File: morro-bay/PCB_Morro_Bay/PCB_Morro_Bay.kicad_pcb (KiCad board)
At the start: 2 copper layers, 220 x 145.5 mm, 344 parts, among them J1 POWER, J10 5V_12_8, J11 5V_12_9, J12 5V_12_10, J13 5V_12_11, J14 5V_12_12, J15 5V_12_13, J16 5V_12_14, J17 10V_12_1, J18 10V_12_2, J19 10V_12_3, J2 CAN, J20 10V_12_4, J21 10V_12_5, J22 10V_12_6, J23 POWER_OUT, J24 5V_16_1, J25 5V_16_2, J26 5V_16_3, J27 5V_16_4, J28 10V_16_1, J29 10V_16_2, J3 5V_12_1, J30 10V_16_3, J31 10V_16_4, J32 5V_16_5, J33 5V_16_6, J34 5V_16_7, J35 5V_16_8, J36 SWD, J37 GPIO, J38 USB_B, J39 ESERCOM, J4 5V_12_2, J5 5V_12_3, J6 5V_12_4, J7 5V_12_5, J8 5V_12_6, J9 5V_12_7, SW1 INPUT_RANGE_SEL_1, SW2 INPUT_RANGE_SEL_2, SW3 RESET, SW4 INPUT_RANGE_SEL_3, U1 MCP2515-xSO, U10 LM2902, U11 LM2902, U12 LM2902, U13 V7805-2000R, U2 SN65HVD232, U26 ADS114S08BIPBSR, U3 AZ1117-3.3, U4 ATSAMD21J18A-AU, U5 LM2902, U6 LM2902, U7 LM2902, U8 LM2902, U9 LM2902, Y1 8MHz, Y2 30MHz, Y3 32.768kHz

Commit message: Silkscreened
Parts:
- added G***: LOGO, PCB_Morro_Bay:M_Logo, B.Cu at (199.2, 84.5)
- added G***: LOGO, PCB_Morro_Bay:P_Logo_Small, F.Cu at (235.0, 171.2)
- moved G*** 173.9 mm to (256.2, 172.8)
- moved J36 99.1 mm to (152.2, 101.6)
- moved R118 99.1 mm to (157.2, 123.8)
- moved C1 99.1 mm to (141.2, 121.8)
- moved C10 99.1 mm to (186.2, 130.2)
- moved C11 99.1 mm to (209.0, 130.2)
- moved C12 99.1 mm to (190.8, 124.2)
- moved C13 99.1 mm to (167.5, 114.5)
- moved C14 99.1 mm to (167.5, 119.0)
- moved C15 99.1 mm to (177.0, 116.8)
- moved C16 99.1 mm to (167.5, 120.8)
- moved C17 99.1 mm to (168.5, 128.8)
- moved C18 99.1 mm to (170.5, 135.2)
- moved C19 99.1 mm to (168.8, 135.2)
- moved C2 99.1 mm to (161.0, 118.2)
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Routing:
- net /SAMD_nRESET: track 45.9 -> 46.9 mm
- net GND: vias 208 -> 209
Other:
- board text added: "Morro Bay SN: Data Acquisition Board"
- board text removed: "Morro Bay Data Acquisition Board"

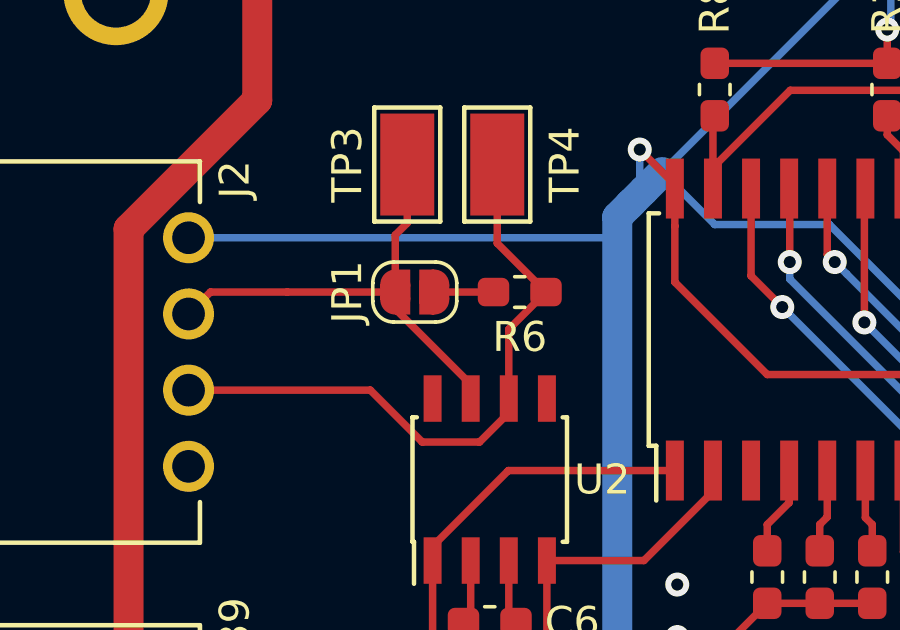
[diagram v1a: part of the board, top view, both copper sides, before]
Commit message: Add CAN termination marking
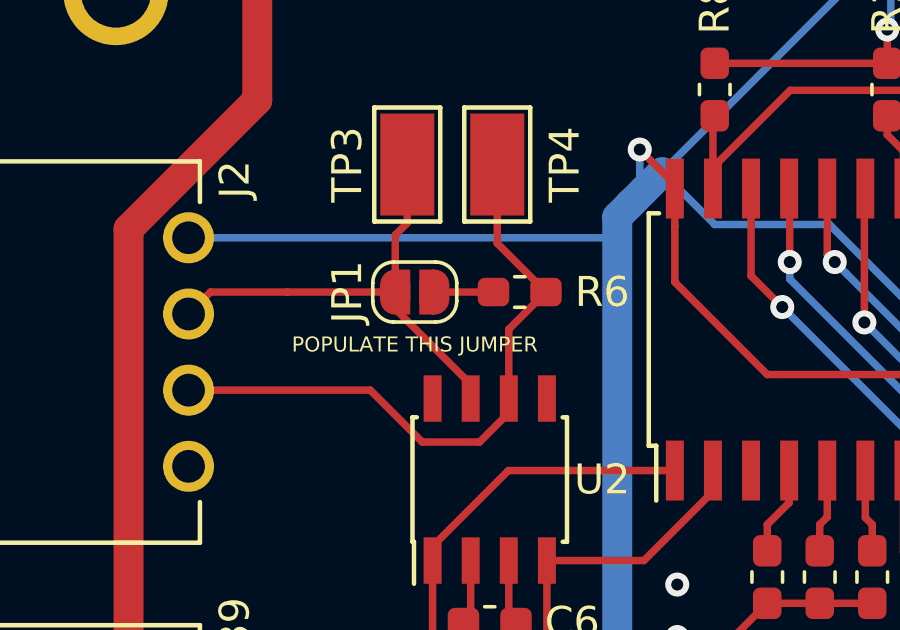
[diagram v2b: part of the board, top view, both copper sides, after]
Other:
- board text added: "POPULATE THIS JUMPER"
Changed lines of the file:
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@@
   (general
     (thickness 1.6)
-    (drawings 15)
+    (drawings 16)
     (tracks 2658)
     (zones 0)
@@
     (tags "resistor handsolder")
     (attr smd)
-    (fp_text reference R6 (at 0 1.5 180) (layer F.SilkS)
+    (fp_text reference R6 (at 2.75 0 180) (layer F.SilkS)
       (effects (font (size 1 1) (thickness 0.15)))
     )
@@
     (pad 4 smd rect (at 3.15 0.45) (size 1.2 0.6) (layers F.Cu F.Paste F.Mask))
   )
+  (gr_text "POPULATE THIS JUMPER" (at 122 109.75) (layer F.SilkS)
+    (effects (font (size 0.5 0.5) (thickness 0.1)))
+  )
   (dimension 131.5 (width 0.15) (layer F.Fab)

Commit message: #justiceforsvideo
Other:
- board text added: "#justiceforsvideo"
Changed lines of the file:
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@@
   (general
     (thickness 1.6)
-    (drawings 16)
+    (drawings 17)
     (tracks 2658)
     (zones 0)
@@
     (pad 4 smd rect (at 3.15 0.45) (size 1.2 0.6) (layers F.Cu F.Paste F.Mask))
   )
+  (gr_text "#justiceforsvideo" (at 174.75 186.5) (layer B.SilkS)
+    (effects (font (size 1 1) (thickness 0.15)) (justify mirror))
+  )
   (gr_text "POPULATE THIS JUMPER" (at 122 109.75) (layer F.SilkS)

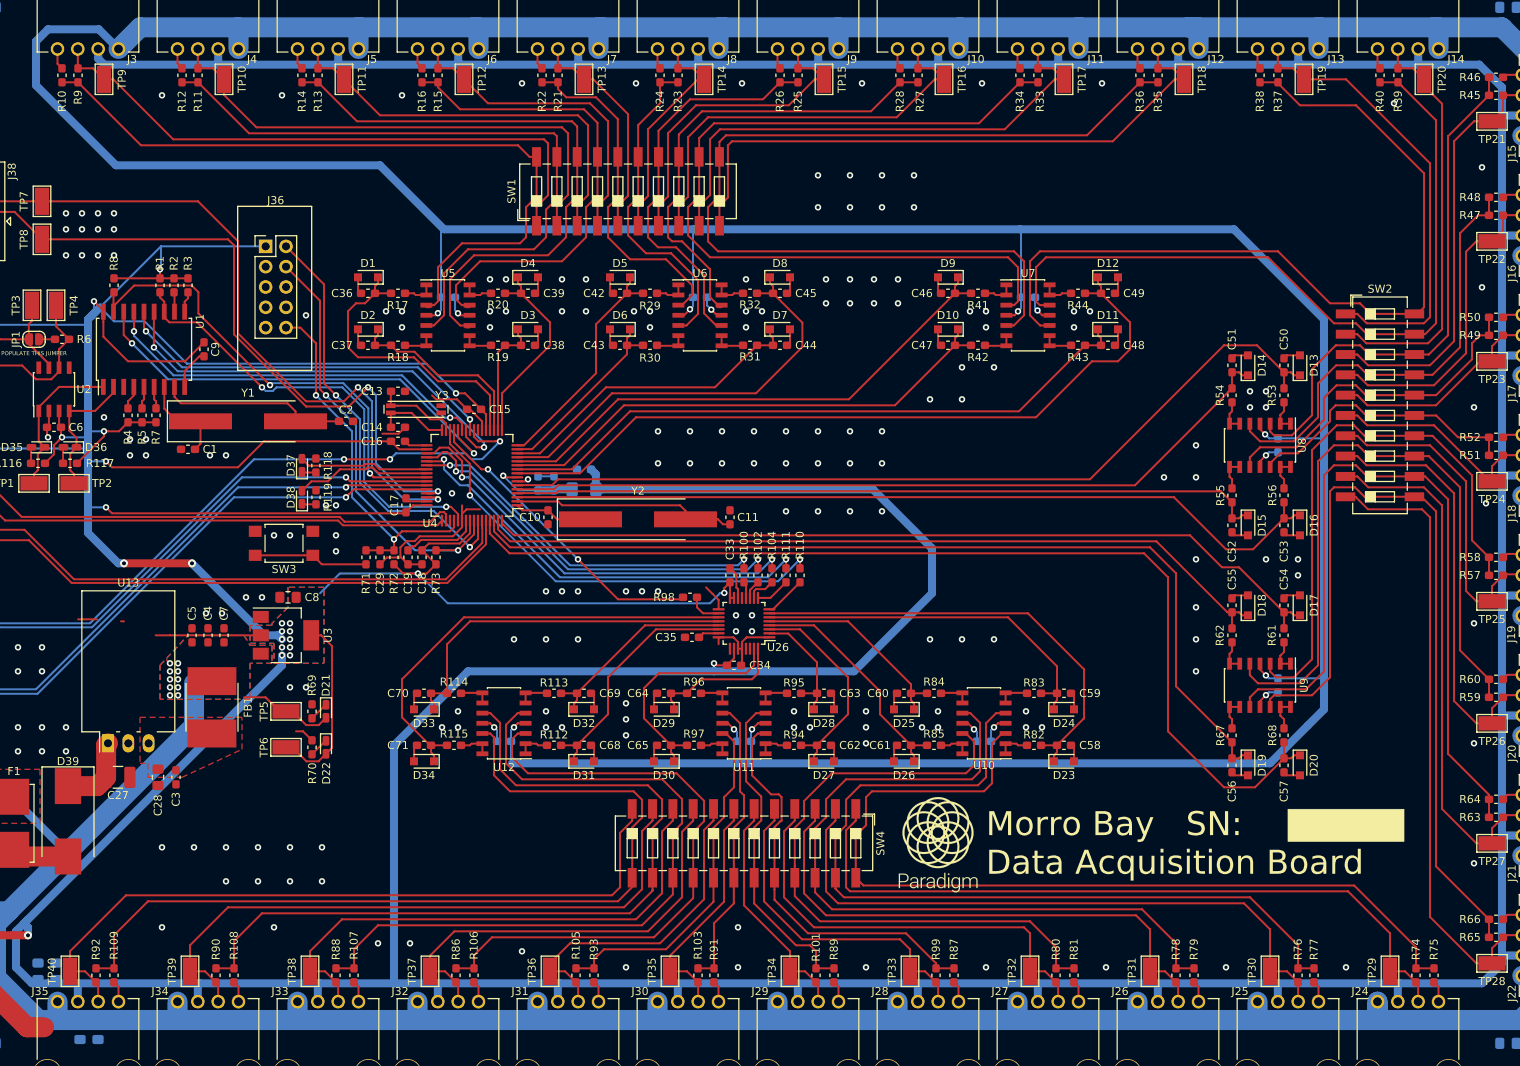
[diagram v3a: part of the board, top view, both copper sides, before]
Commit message: Update from Fronk's review
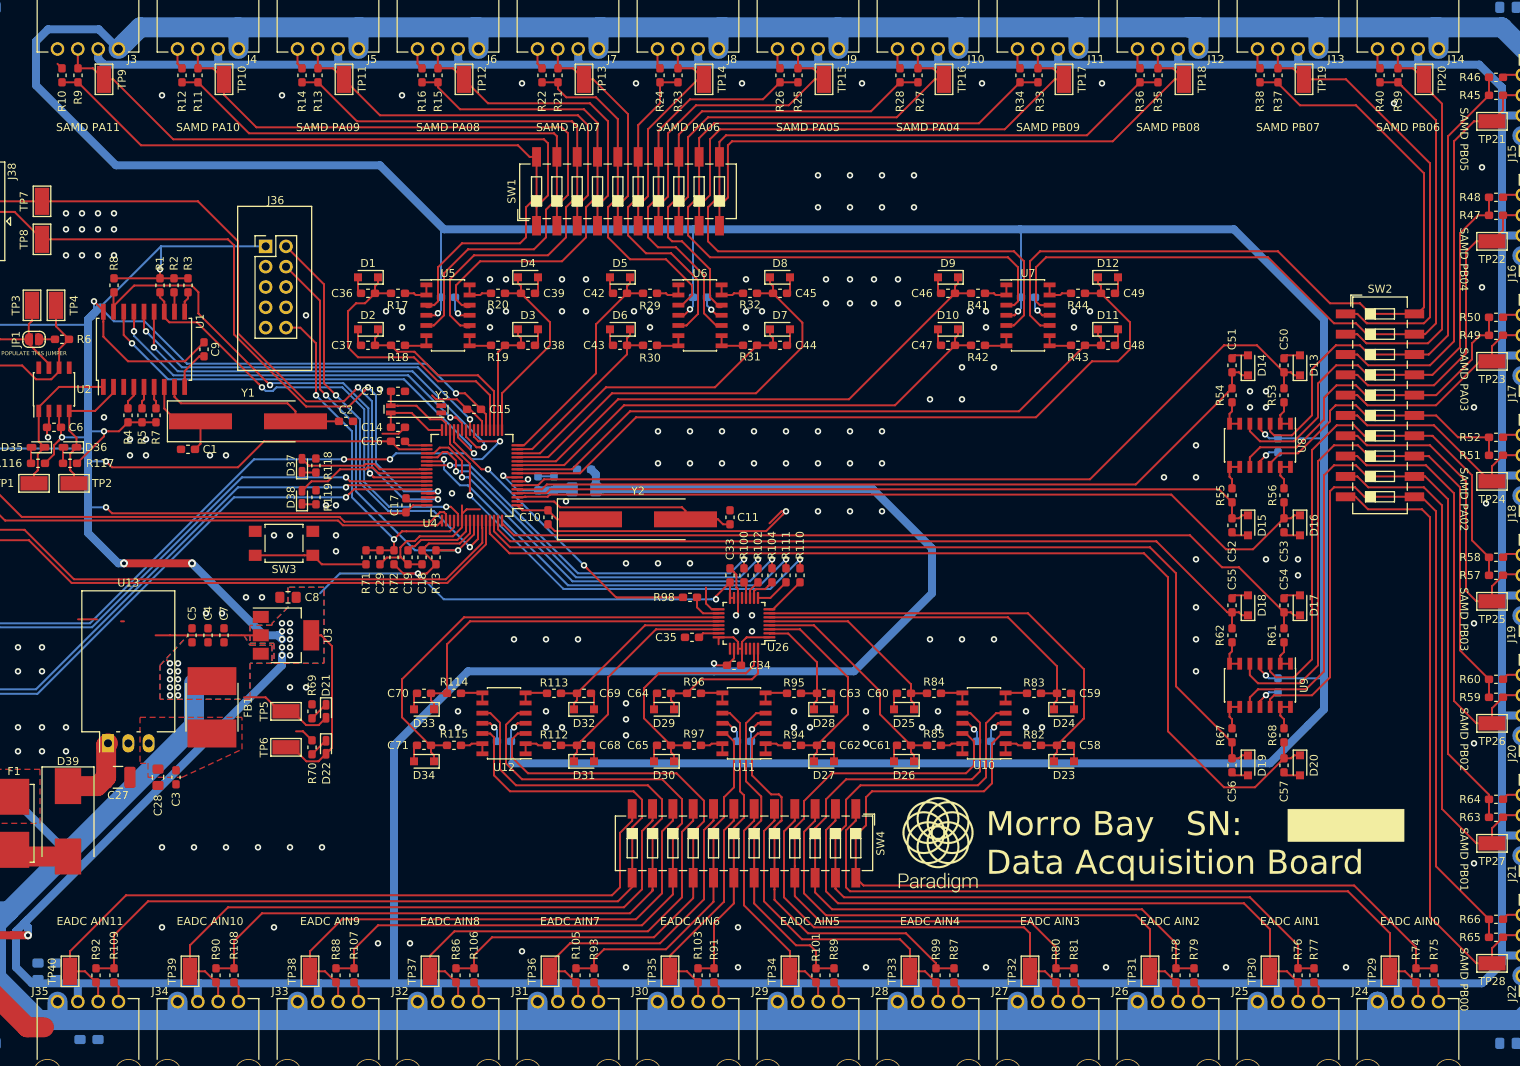
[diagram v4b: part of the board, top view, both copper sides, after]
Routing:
- net GND: track 275.1 -> 309.8 mm, vias 209 -> 204
- net EADC_SCLK: track 50.2 -> 51.0 mm
- net EADC_DIN: track 53.0 -> 53.9 mm
- net EADC_DOUT_DRDY: track 46.3 -> 47.1 mm
- net EADC_CS: track 53.9 -> 54.7 mm
- net EADC_START_SYNC: track 57.2 -> 58.0 mm
- net +3V3: track 1200.1 -> 1199.5 mm
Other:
- board text added: "EADC AIN0"
- board text added: "EADC AIN1"
- board text added: "EADC AIN10"
- board text added: "EADC AIN11"
- board text added: "EADC AIN2"
- board text added: "EADC AIN3"
- board text added: "EADC AIN4"
- board text added: "EADC AIN5"
- board text added: "EADC AIN6"
- board text added: "EADC AIN7"
- board text added: "EADC AIN8"
- board text added: "EADC AIN9"
- board text added: "SAMD PA02"
- board text added: "SAMD PA03"
- board text added: "SAMD PA04"
- board text added: "SAMD PA05"
- board text added: "SAMD PA06"
- board text added: "SAMD PA07"
- board text added: "SAMD PA08"
- board text added: "SAMD PA09"
- board text added: "SAMD PA10"
- board text added: "SAMD PA11"
- board text added: "SAMD PB00"
- board text added: "SAMD PB01"
- board text added: "SAMD PB02"
- board text added: "SAMD PB03"
- board text added: "SAMD PB04"
- board text added: "SAMD PB05"
- board text added: "SAMD PB06"
- board text added: "SAMD PB07"
- board text added: "SAMD PB08"
- board text added: "SAMD PB09"

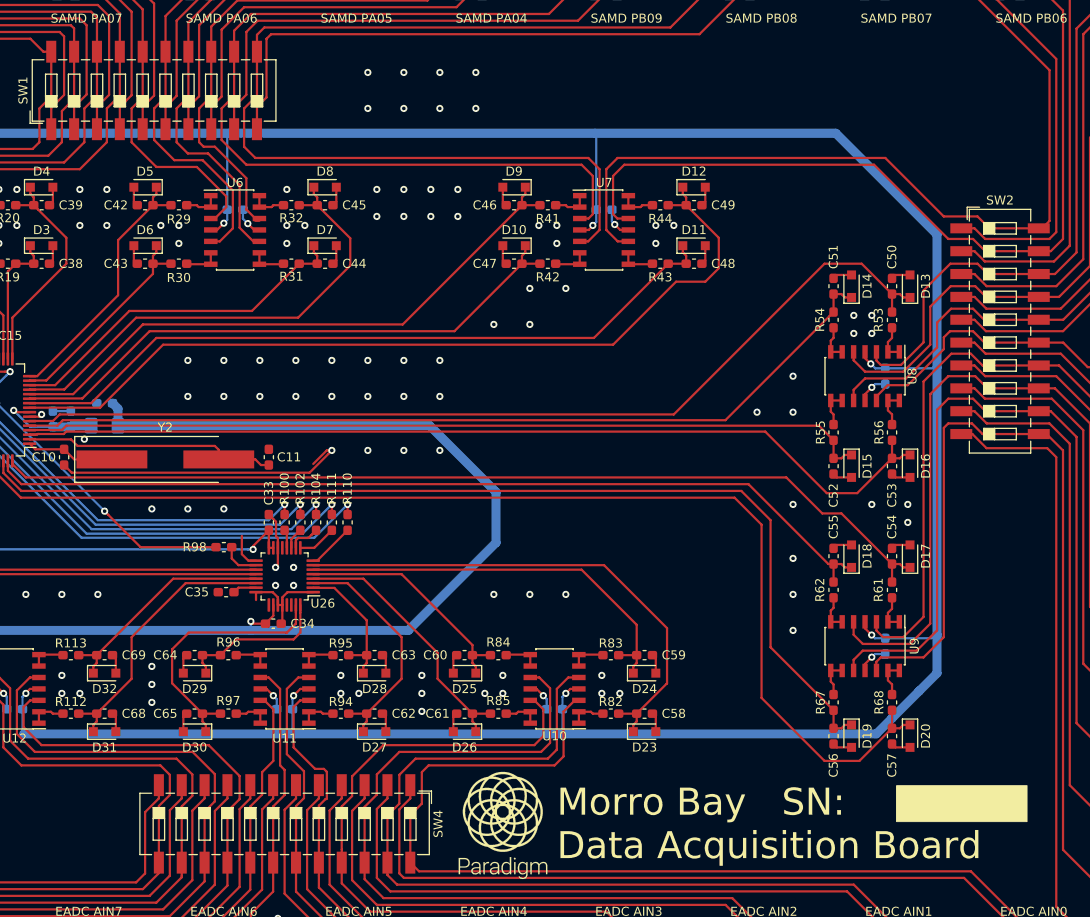
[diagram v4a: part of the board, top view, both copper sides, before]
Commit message: Add direction silkscreen for DIP switches
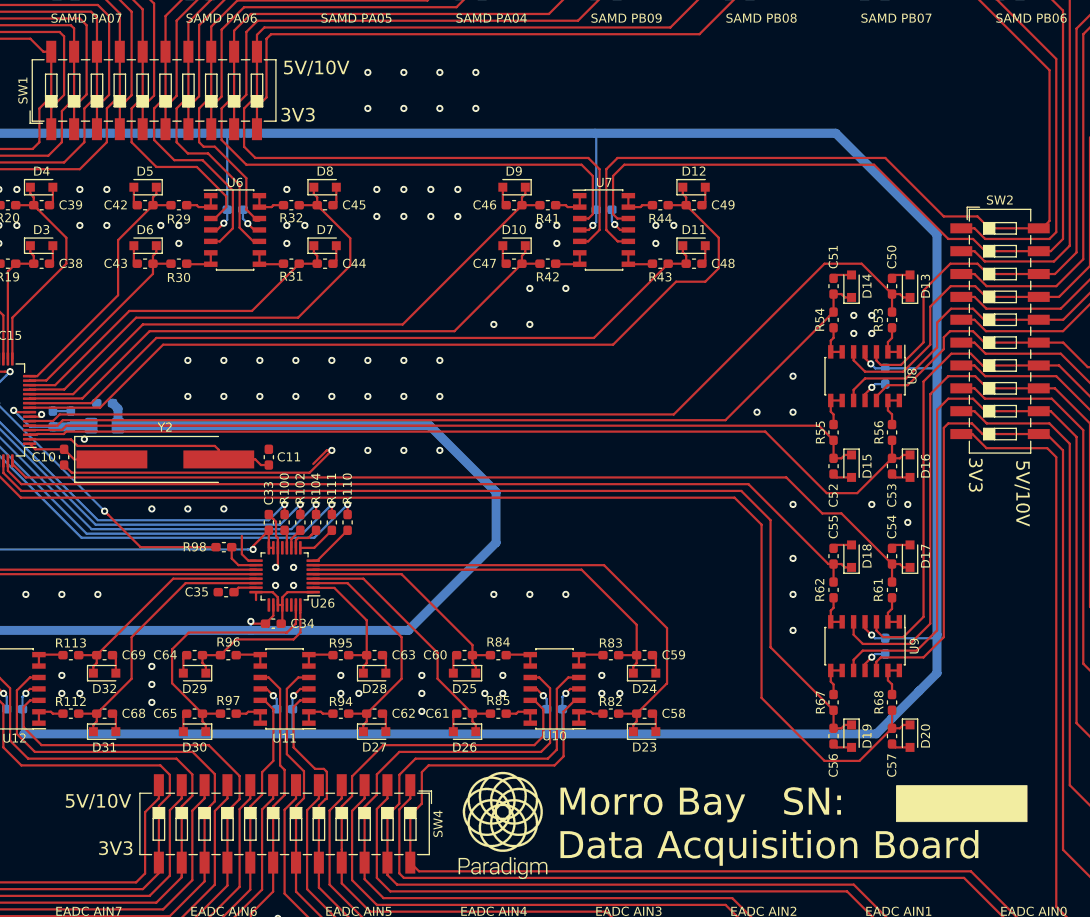
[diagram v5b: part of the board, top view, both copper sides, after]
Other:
- board text added: "3V3"
- board text added: "5V/10V"
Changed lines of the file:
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@@
   (general
     (thickness 1.6)
-    (drawings 49)
+    (drawings 57)
     (tracks 2666)
     (zones 0)
@@
     (pad 4 smd rect (at 3.15 0.45) (size 1.2 0.6) (layers F.Cu F.Paste F.Mask))
   )
+  (gr_text 5V/10V (at 190 168.5) (layer F.SilkS)
+    (effects (font (size 1.5 1.5) (thickness 0.3)))
+  )
+  (gr_text 3V3 (at 192 173.75) (layer F.SilkS)
+    (effects (font (size 1.5 1.5) (thickness 0.3)))
+  )
+  (gr_text 5V/10V (at 292.75 134.25 270) (layer F.SilkS)
+    (effects (font (size 1.5 1.5) (thickness 0.3)))
+  )
+  (gr_text 3V3 (at 287.5 132.25 270) (layer F.SilkS)
+    (effects (font (size 1.5 1.5) (thickness 0.3)))
+  )
+  (gr_text 3V3 (at 212.25 92.25) (layer F.SilkS)
+    (effects (font (size 1.5 1.5) (thickness 0.3)))
+  )
+  (gr_text 5V/10V (at 214.25 87) (layer F.SilkS)
+    (effects (font (size 1.5 1.5) (thickness 0.3)))
+  )
+  (dimension 7 (width 0.12) (layer Dwgs.User)
+    (gr_text "7.000 mm" (at 95.23 62 90) (layer Dwgs.User)
+      (effects (font (size 1 1) (thickness 0.15)))
+    )
+    (feature1 (pts (xy 108.25 58.5) (xy 95.913579 58.5)))
+    (feature2 (pts (xy 108.25 65.5) (xy 95.913579 65.5)))
+    (crossbar (pts (xy 96.5 65.5) (xy 96.5 58.5)))
+    (arrow1a (pts (xy 96.5 58.5) (xy 97.086421 59.626504)))
+    (arrow1b (pts (xy 96.5 58.5) (xy 95.913579 59.626504)))
+    (arrow2a (pts (xy 96.5 65.5) (xy 97.086421 64.373496)))
+    (arrow2b (pts (xy 96.5 65.5) (xy 95.913579 64.373496)))
+  )
+  (dimension 7 (width 0.12) (layer Dwgs.User)
+    (gr_text "7.000 mm" (at 104.75 48.48) (layer Dwgs.User)
+      (effects (font (size 1 1) (thickness 0.15)))
+    )
+    (feature1 (pts (xy 101.25 65.5) (xy 101.25 49.163579)))
+    (feature2 (pts (xy 108.25 65.5) (xy 108.25 49.163579)))
+    (crossbar (pts (xy 108.25 49.75) (xy 101.25 49.75)))
+    (arrow1a (pts (xy 101.25 49.75) (xy 102.376504 49.163579)))
+    (arrow1b (pts (xy 101.25 49.75) (xy 102.376504 50.336421)))
+    (arrow2a (pts (xy 108.25 49.75) (xy 107.123496 49.163579)))
+    (arrow2b (pts (xy 108.25 49.75) (xy 107.123496 50.336421)))
+  )
   (gr_text "EADC AIN8" (at 174 180.75) (layer F.SilkS)
